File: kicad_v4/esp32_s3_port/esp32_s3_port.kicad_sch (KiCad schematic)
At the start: 50 parts, among them J1 AudioJack4, J2 AudioJack4, SW1 KS33_SW_HS, SW10 KS33_SW_HS, SW11 KS33_SW_HS, SW12 KS33_SW_HS, SW13 KS33_SW_HS, SW14 KS33_SW_HS, SW15 KS33_SW_HS, SW16 KS33_SW_HS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

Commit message: ssd 1306
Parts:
- removed U4: SSD1306-128X64-OLED-0.96, Library:SSD1306, symbol Library:SSD1306-128X64-OLED-0.96
- added Brd1: SSD1306, SSD1306:128x64OLED, symbol ssd1306:SSD1306
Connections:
- net GND: now also Brd1.1 (GND)
- net SCL: now also Brd1.3 (SCL)
- net SDA: now also Brd1.4 (SDA)
- net VCC: now also Brd1.2 (VCC)
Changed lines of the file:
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@@
 	(wire
 		(pts
+			(xy 153.67 121.92) (xy 153.67 127)
+		)
+		(stroke
+			(width 0)
+			(type default)
+		)
+	)
+	(wire
+		(pts
 			(xy 52.07 160.02) (xy 52.07 179.07)
 		)
@@
 	(wire
 		(pts
+			(xy 147.32 127) (xy 151.13 127)
+		)
+		(stroke
+			(width 0)
+			(type default)
+		)
+	)
+	(wire
+		(pts
 			(xy 82.55 172.72) (xy 95.25 172.72)
 		)
@@
 		)
 	)
-	(global_label "SDA"
+	(global_label "RX"
 		(shape input)
-		(at 151.13 140.97 180)
+		(at 156.21 69.85 180)
 		(fields_autoplaced yes)
 		(effects
@@
 		)
 		(property "Intersheetrefs" "${INTERSHEET_REFS}"
-			(at 144.5767 140.97 0)
+			(at 150.7453 69.85 0)
 			(effects
 				(font
@@
 		)
 	)
-	(global_label "RX"
+	(global_label "SCL"
 		(shape input)
-		(at 156.21 69.85 180)
+		(at 156.21 127 90)
 		(fields_autoplaced yes)
 		(effects
@@
 				(size 1.27 1.27)
 			)
-			(justify right)
+			(justify left)
 		)
 		(property "Intersheetrefs" "${INTERSHEET_REFS}"
-			(at 150.7453 69.85 0)
+			(at 156.21 120.5072 90)
 			(effects
 				(font
 					(size 1.27 1.27)
 				)
-				(justify right)
+				(justify left)
 				(hide yes)
 			)
@@
 		)
 	)
-	(global_label "RX"
+	(global_label "SDA"
 		(shape input)
-		(at 106.68 86.36 0)
+		(at 158.75 127 90)
 		(fields_autoplaced yes)
 		(effects
@@
 		)
 		(property "Intersheetrefs" "${INTERSHEET_REFS}"
-			(at 112.1447 86.36 0)
+			(at 158.75 120.4467 90)
 			(effects
 				(font
@@
 		)
 	)
-	(global_label "TX"
+	(global_label "RX"
 		(shape input)
-		(at 106.68 68.58 0)
+		(at 106.68 86.36 0)
 		(fields_autoplaced yes)
 		(effects
@@
 		)
 		(property "Intersheetrefs" "${INTERSHEET_REFS}"
-			(at 111.8423 68.58 0)
+			(at 112.1447 86.36 0)
 			(effects
 				(font
@@
 		)
 	)
-	(global_label "SCL"
+	(global_label "TX"
 		(shape input)
-		(at 151.13 138.43 180)
+		(at 106.68 68.58 0)
 		(fields_autoplaced yes)
 		(effects
@@
 				(size 1.27 1.27)
 			)
-			(justify right)
+			(justify left)
 		)
 		(property "Intersheetrefs" "${INTERSHEET_REFS}"
-			(at 144.6372 138.43 0)
+			(at 111.8423 68.58 0)
 			(effects
 				(font
 					(size 1.27 1.27)
 				)
-				(justify right)
+				(justify left)
 				(hide yes)
 			)
@@
 	)
 	(symbol
-		(lib_id "Library:SSD1306-128X64-OLED-0.96")
-		(at 158.75 140.97 0)
-		(unit 1)
-		(exclude_from_sim no)
-		(in_bom yes)
-		(on_board yes)
-		(dnp no)
-		(fields_autoplaced yes)
-		(property "Reference" "U4"
-			(at 170.18 139.6999 0)
-			(effects
-				(font
-					(size 1.27 1.27)
-				)
-				(justify left)
-			)
-		)
-		(property "Value" "SSD1306-128X64-OLED-0.96"
-			(at 162.052 151.892 0)
-			(effects
-				(font
-					(size 1.27 1.27)
-				)
-				(hide yes)
-			)
-		)
-		(property "Footprint" "Library:SSD1306"
-			(at 160.782 128.778 0)
-			(effects
-				(font
-					(size 1.27 1.27)
-				)
-				(hide yes)
-			)
-		)
-		(property "Datasheet" ""
-			(at 158.75 140.97 0)
-			(effects
-				(font
-					(size 1.27 1.27)
-				)
-				(hide yes)
-			)
-		)
-		(property "Description" ""
-			(at 158.75 140.97 0)
-			(effects
-				(font
-					(size 1.27 1.27)
-				)
-				(hide yes)
-			)
-		)
-		(pin "2"
-		)
-		(pin "1"
-		)
-		(pin "3"
-		)
-		(pin "4"
-		)
-		(instances
-			(project "esp32_s3_port"
-				(path "/b35913c0-3727-49b0-a8b1-477815153830"
-					(reference "U4")
-					(unit 1)
-				)
-			)
-		)
-	)
-	(symbol
 		(lib_id "Device:Battery_Cell")
 		(at 236.22 144.78 0)
@@
 	(symbol
 		(lib_id "power:GND")
-		(at 151.13 146.05 0)
+		(at 147.32 127 0)
 		(unit 1)
 		(exclude_from_sim no)
@@
 		(fields_autoplaced yes)
 		(property "Reference" "#PWR016"
-			(at 151.13 152.4 0)
+			(at 147.32 133.35 0)
 			(effects
 				(font
@@
 		)
 		(property "Value" "GND"
-			(at 151.13 151.13 0)
+			(at 147.32 132.08 0)
 			(effects
 				(font
@@
 		)
 		(property "Footprint" ""
-			(at 151.13 146.05 0)
+			(at 147.32 127 0)
 			(effects
 				(font
@@
 		)
 		(property "Datasheet" ""
-			(at 151.13 146.05 0)
+			(at 147.32 127 0)
 			(effects
 				(font
@@
 		)
 		(property "Description" "Power symbol creates a global label with name \"GND\" , ground"
-			(at 151.13 146.05 0)
+			(at 147.32 127 0)
 			(effects
 				(font
@@
 	(symbol
 		(lib_id "power:VCC")
-		(at 151.13 133.35 0)
+		(at 153.67 121.92 0)
 		(unit 1)
 		(exclude_from_sim no)
@@
 		(fields_autoplaced yes)
 		(property "Reference" "#PWR05"
-			(at 151.13 137.16 0)
+			(at 153.67 125.73 0)
 			(effects
 				(font
@@
 		)
 		(property "Value" "VCC"
-			(at 151.13 128.27 0)
+			(at 153.67 116.84 0)
 			(effects
 				(font
@@
 		)
 		(property "Footprint" ""
-			(at 151.13 133.35 0)
+			(at 153.67 121.92 0)
 			(effects
 				(font
@@
 		)
 		(property "Datasheet" ""
-			(at 151.13 133.35 0)
+			(at 153.67 121.92 0)
 			(effects
 				(font
@@
 		)
 		(property "Description" "Power symbol creates a global label with name \"VCC\""
-			(at 151.13 133.35 0)
+			(at 153.67 121.92 0)
 			(effects
 				(font
@@
 					(unit 1)
 				)
+			)
+		)
+	)
+	(symbol
+		(lib_id "ssd1306:SSD1306")
+		(at 154.94 135.89 0)
+		(unit 1)
+		(exclude_from_sim no)
+		(in_bom yes)
+		(on_board yes)
+		(dnp no)
+		(fields_autoplaced yes)
+		(property "Reference" "Brd1"
+			(at 162.56 134.6199 0)
+			(effects
+				(font
+					(size 1.27 1.27)
+				)
+				(justify left)
+			)
+		)
+		(property "Value" "SSD1306"
+			(at 162.56 137.1599 0)
+			(effects
+				(font
+					(size 1.27 1.27)
+				)
+				(justify left)
+			)
+		)
+		(property "Footprint" "SSD1306:128x64OLED"
+			(at 154.94 129.54 0)
+			(effects
+				(font
+					(size 1.27 1.27)
+				)
+				(hide yes)
+			)
+		)
+		(property "Datasheet" ""
+			(at 154.94 129.54 0)
+			(effects
+				(font
+					(size 1.27 1.27)
+				)
+				(hide yes)
+			)
+		)
+		(property "Description" "SSD1306 OLED"
+			(at 154.94 135.89 0)
+			(effects
+				(font
+					(size 1.27 1.27)
+				)
+				(hide yes)
+			)
+		)
+		(pin "3"
+		)
+		(pin "1"
+		)
+		(pin "2"
+		)
+		(pin "4"
+		)
+		(instances
+			(project ""
+				(path "/b35913c0-3727-49b0-a8b1-477815153830"
+					(reference "Brd1")
+					(unit 1)
+				)

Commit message: battery switch
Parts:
- added SW22: Slide_Switch_SPDT_P3mm_10x5x10mm, PCM_SL_Devices:Slide_Switch_SPDT_P3mm_10x5x10mm, symbol PCM_SL_Devices:Slide_Switch_SPDT_P3mm_10x5x10mm
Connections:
- net at BT1.1 (+), JP1.1: now also SW22.2; no longer U1.3 (BAT)
- new net: SW22.1, U1.3 (BAT)
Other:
- moved on the sheet: BT1, JP1
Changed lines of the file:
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@@
 	)
 	(junction
-		(at 231.14 139.7)
-		(diameter 0)
-		(color 0 0 0 0)
-	)
-	(junction
 		(at 44.45 172.72)
 		(diameter 0)
@@
 	)
 	(junction
+		(at 243.84 138.43)
+		(diameter 0)
+		(color 0 0 0 0)
+	)
+	(junction
 		(at 69.85 137.16)
 		(diameter 0)
@@
 	)
 	(junction
-		(at 236.22 147.32)
+		(at 246.38 146.05)
 		(diameter 0)
 		(color 0 0 0 0)
@@
 	(wire
 		(pts
+			(xy 243.84 137.16) (xy 243.84 138.43)
+		)
+		(stroke
+			(width 0)
+			(type default)
+		)
+	)
+	(wire
+		(pts
 			(xy 26.67 140.97) (xy 26.67 160.02)
 		)
@@
 	(wire
 		(pts
+			(xy 243.84 138.43) (xy 246.38 138.43)
+		)
+		(stroke
+			(width 0)
+			(type default)
+		)
+	)
+	(wire
+		(pts
 			(xy 156.21 72.39) (xy 161.29 72.39)
 		)
@@
 	(wire
 		(pts
-			(xy 231.14 139.7) (xy 236.22 139.7)
+			(xy 241.3 138.43) (xy 243.84 138.43)
 		)
 		(stroke
@@
 	(wire
 		(pts
-			(xy 220.98 139.7) (xy 231.14 139.7)
+			(xy 69.85 153.67) (xy 82.55 153.67)
 		)
 		(stroke
@@
 	(wire
 		(pts
-			(xy 69.85 153.67) (xy 82.55 153.67)
+			(xy 31.75 172.72) (xy 44.45 172.72)
 		)
 		(stroke
@@
 	(wire
 		(pts
-			(xy 31.75 172.72) (xy 44.45 172.72)
+			(xy 52.07 115.57) (xy 52.07 124.46)
 		)
 		(stroke
@@
 	(wire
 		(pts
-			(xy 52.07 115.57) (xy 52.07 124.46)
+			(xy 39.37 114.3) (xy 39.37 124.46)
 		)
 		(stroke
@@
 	(wire
 		(pts
-			(xy 39.37 114.3) (xy 39.37 124.46)
+			(xy 69.85 137.16) (xy 82.55 137.16)
 		)
 		(stroke
@@
 	(wire
 		(pts
-			(xy 69.85 137.16) (xy 82.55 137.16)
+			(xy 64.77 124.46) (xy 64.77 140.97)
 		)
 		(stroke
@@
 	(wire
 		(pts
-			(xy 64.77 124.46) (xy 64.77 140.97)
+			(xy 232.41 137.16) (xy 243.84 137.16)
 		)
 		(stroke
@@
 	(wire
 		(pts
-			(xy 231.14 147.32) (xy 231.14 146.05)
+			(xy 241.3 146.05) (xy 241.3 144.78)
 		)
 		(stroke
@@
 	(wire
 		(pts
-			(xy 231.14 139.7) (xy 231.14 140.97)
+			(xy 241.3 138.43) (xy 241.3 139.7)
 		)
 		(stroke
@@
 	(wire
 		(pts
-			(xy 236.22 149.86) (xy 236.22 147.32)
+			(xy 246.38 148.59) (xy 246.38 146.05)
 		)
 		(stroke
@@
 	(wire
 		(pts
-			(xy 231.14 147.32) (xy 236.22 147.32)
+			(xy 241.3 146.05) (xy 246.38 146.05)
 		)
 		(stroke
@@
 	(symbol
 		(lib_id "power:GND")
-		(at 236.22 149.86 0)
+		(at 246.38 148.59 0)
 		(unit 1)
 		(exclude_from_sim no)
@@
 		(fields_autoplaced yes)
 		(property "Reference" "#PWR02"
-			(at 236.22 156.21 0)
+			(at 246.38 154.94 0)
 			(effects
 				(font
@@
 		)
 		(property "Value" "GND"
-			(at 236.22 154.94 0)
+			(at 246.38 153.67 0)
 			(effects
 				(font
@@
 		)
 		(property "Footprint" ""
-			(at 236.22 149.86 0)
+			(at 246.38 148.59 0)
 			(effects
 				(font
@@
 		)
 		(property "Datasheet" ""
-			(at 236.22 149.86 0)
+			(at 246.38 148.59 0)
 			(effects
 				(font
@@
 		)
 		(property "Description" "Power symbol creates a global label with name \"GND\" , ground"
-			(at 236.22 149.86 0)
+			(at 246.38 148.59 0)
 			(effects
 				(font
@@
 	(symbol
 		(lib_id "Device:Battery_Cell")
-		(at 236.22 144.78 0)
+		(at 246.38 143.51 0)
 		(unit 1)
 		(exclude_from_sim no)
@@
 		(fields_autoplaced yes)
 		(property "Reference" "BT1"
-			(at 240.03 141.6684 0)
+			(at 250.19 140.3984 0)
 			(effects
 				(font
@@
 		)
 		(property "Value" "Battery_Cell"
-			(at 240.03 144.2084 0)
+			(at 250.19 142.9384 0)
 			(effects
 				(font
@@
 		)
 		(property "Footprint" ""
-			(at 236.22 143.256 90)
+			(at 246.38 141.986 90)
 			(effects
 				(font
@@
 		)
 		(property "Datasheet" "~"
-			(at 236.22 143.256 90)
+			(at 246.38 141.986 90)
 			(effects
 				(font
@@
 		)
 		(property "Description" "Single-cell battery"
-			(at 236.22 144.78 0)
+			(at 246.38 143.51 0)
 			(effects
 				(font
@@
 		(on_board yes)
 		(dnp no)
-		(fields_autoplaced yes)
 		(property "Reference" "R2"
 			(at 226.06 147.3199 90)
@@
 		)
 		(property "Value" "2.2k"
-			(at 226.06 149.8599 90)
+			(at 236.22 148.5899 90)
 			(effects
 				(font
@@
 	(symbol
 		(lib_id "PCM_SL_Jumpers_THT:JUP_P5.08mm")
-		(at 231.14 143.51 270)
+		(at 241.3 142.24 270)
 		(unit 1)
 		(exclude_from_sim no)
@@
 		(fields_autoplaced yes)
 		(property "Reference" "JP1"
-			(at 232.41 142.24 90)
+			(at 242.57 140.97 90)
 			(effects
 				(font
@@
 		)
 		(property "Value" "JUP_P5.08mm"
-			(at 232.41 144.78 90)
+			(at 242.57 143.51 90)
 			(effects
 				(font
@@
 		)
 		(property "Footprint" "PCM_SL_Jumpers:JUP_P5.08mm"
-			(at 231.14 143.51 0)
+			(at 241.3 142.24 0)
 			(effects
 				(font
@@
 		)
 		(property "Datasheet" ""
-			(at 231.14 143.51 0)
+			(at 241.3 142.24 0)
 			(effects
 				(font
@@
 		)
 		(property "Description" "Through-Hole Jumpers or wire links with a pin space of 5.08mm"
-			(at 231.14 143.51 0)
+			(at 241.3 142.24 0)
 			(effects
 				(font
@@
 					(unit 1)
 				)
+			)
+		)
+	)
+	(symbol
+		(lib_id "PCM_SL_Devices:Slide_Switch_SPDT_P3mm_10x5x10mm")
+		(at 227.33 139.7 0)
+		(unit 1)
+		(exclude_from_sim no)
+		(in_bom yes)
+		(on_board yes)
+		(dnp no)
+		(fields_autoplaced yes)
+		(property "Reference" "SW22"
+			(at 226.695 132.08 0)
+			(effects
+				(font
+					(size 1.27 1.27)
+				)
+			)
+		)
+		(property "Value" "Slide_Switch_SPDT_P3mm_10x5x10mm"
+			(at 226.695 134.62 0)
+			(effects
+				(font
+					(size 1.27 1.27)
+				)
+			)
+		)
+		(property "Footprint" "PCM_SL_Devices:Slide_Switch_SPDT_P3mm_10x5x10mm"
+			(at 228.6 147.32 0)
+			(effects
+				(font
+					(size 1.27 1.27)
+				)
+				(hide yes)
+			)
+		)
+		(property "Datasheet" ""
+			(at 226.06 133.35 0)
+			(effects
+				(font
+					(size 1.27 1.27)
+				)
+				(hide yes)
+			)
+		)
+		(property "Description" "SPDT Slide Switch with 10mm length, 5mm width and 10mm hight."
+			(at 227.33 139.7 0)
+			(effects
+				(font
+					(size 1.27 1.27)
+				)
+				(hide yes)
+			)
+		)
+		(pin "1"
+		)
+		(pin "2"
+		)
+		(pin "3"
+		)
+		(instances
+			(project ""
+				(path "/b35913c0-3727-49b0-a8b1-477815153830"
+					(reference "SW22")
+					(unit 1)
+				)

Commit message: updates
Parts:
- removed BT1: Battery_Cell, symbol Device:Battery_Cell
- removed J1, J2: AudioJack4, PJ-320A_Library:PJ-320A, symbol TRRS:AudioJack4
- removed JP1: JUP_P5.08mm, PCM_SL_Jumpers:JUP_P5.08mm, symbol PCM_SL_Jumpers_THT:JUP_P5.08mm
- added J1: Battery, Connector_PinHeader_2.54mm:PinHeader_1x02_P2.54mm_Vertical, symbol PCM_SL_Pin_Headers:PINHD_1x2_Male
- added J3: misc Pogo pin connector, Connector_PinHeader_2.54mm:PinHeader_1x04_P2.54mm_Vertical, symbol PCM_SL_Pin_Headers:PINHD_1x4_Male
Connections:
- net GND: now also J1.2, J3.4
- net SCL: now also J3.2
- net SDA: now also J3.3
- net VCC: now also J3.1
- net at SW22.2: now also J1.1
- net RX: no longer names the net of A1.2 (D0/RX)
- net TX: no longer names the net of A1.1 (D1/TX)
- net VBUS: no longer names the net of A1.27 (VUSB/5V)
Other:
- moved on the sheet: A1, Brd1, D1, D10, D11, D12, D13, D14, D15, D16, D17, D18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

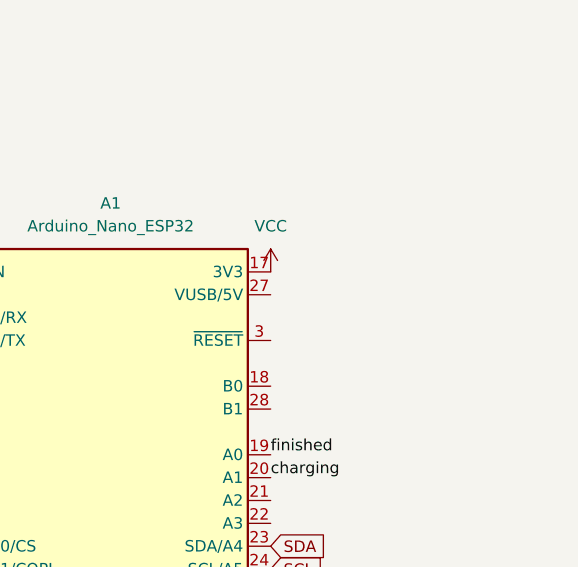
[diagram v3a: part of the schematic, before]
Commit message: hardware update
lots of items were switced with the equivalent headers
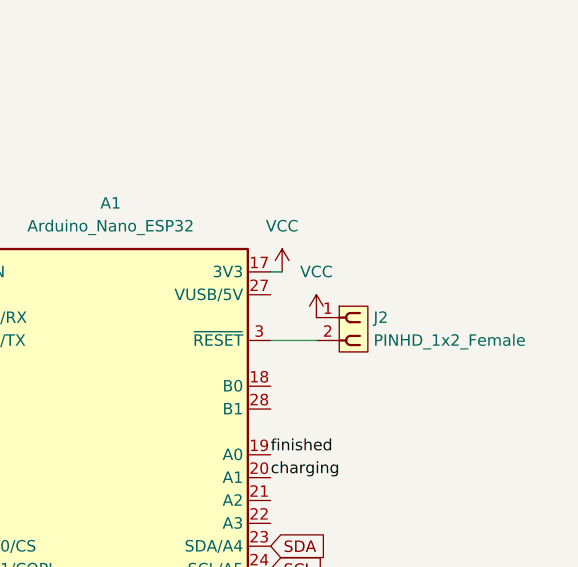
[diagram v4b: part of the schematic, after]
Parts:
- added J2: PINHD_1x2_Female, Connector_PinSocket_2.54mm:PinSocket_1x02_P2.54mm_Vertical, symbol PCM_SL_Pin_Headers:PINHD_1x2_Female
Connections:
- net VCC: now also J2.1
- net at A1.3 (~{RESET}): now also J2.2
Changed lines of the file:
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@@
 	(wire
 		(pts
+			(xy 237.49 82.55) (xy 242.57 82.55)
+		)
+		(stroke
+			(width 0)
+			(type default)
+		)
+	)
+	(wire
+		(pts
 			(xy 139.7 22.86) (xy 139.7 25.4)
 		)
@@
 	(wire
 		(pts
+			(xy 238.76 74.93) (xy 237.49 74.93)
+		)
+		(stroke
+			(width 0)
+			(type default)
+		)
+	)
+	(wire
+		(pts
 			(xy 69.85 77.47) (xy 82.55 77.47)
 		)
@@
 	)
 	(symbol
+		(lib_id "power:VCC")
+		(at 242.57 80.01 0)
+		(unit 1)
+		(exclude_from_sim no)
+		(in_bom yes)
+		(on_board yes)
+		(dnp no)
+		(fields_autoplaced yes)
+		(property "Reference" "#PWR08"
+			(at 242.57 83.82 0)
+			(effects
+				(font
+					(size 1.27 1.27)
+				)
+				(hide yes)
+			)
+		)
+		(property "Value" "VCC"
+			(at 242.57 74.93 0)
+			(effects
+				(font
+					(size 1.27 1.27)
+				)
+			)
+		)
+		(property "Footprint" ""
+			(at 242.57 80.01 0)
+			(effects
+				(font
+					(size 1.27 1.27)
+				)
+				(hide yes)
+			)
+		)
+		(property "Datasheet" ""
+			(at 242.57 80.01 0)
+			(effects
+				(font
+					(size 1.27 1.27)
+				)
+				(hide yes)
+			)
+		)
+		(property "Description" "Power symbol creates a global label with name \"VCC\""
+			(at 242.57 80.01 0)
+			(effects
+				(font
+					(size 1.27 1.27)
+				)
+				(hide yes)
+			)
+		)
+		(pin "1"
+		)
+		(instances
+			(project "esp32_s3_port"
+				(path "/b35913c0-3727-49b0-a8b1-477815153830"
+					(reference "#PWR08")
+					(unit 1)
+				)
+			)
+		)
+	)
+	(symbol
 		(lib_id "PCM_marbastlib-gateron_lp:KS33_SW_HS_KS-2P02B01-02")
 		(at 80.01 31.75 0)
@@
 	(symbol
 		(lib_id "power:VCC")
-		(at 237.49 74.93 0)
+		(at 238.76 74.93 0)
 		(unit 1)
 		(exclude_from_sim no)
@@
 		(fields_autoplaced yes)
 		(property "Reference" "#PWR04"
-			(at 237.49 78.74 0)
+			(at 238.76 78.74 0)
 			(effects
 				(font
@@
 		)
 		(property "Value" "VCC"
-			(at 237.49 69.85 0)
+			(at 238.76 69.85 0)
 			(effects
 				(font
@@
 		)
 		(property "Footprint" ""
-			(at 237.49 74.93 0)
+			(at 238.76 74.93 0)
 			(effects
 				(font
@@
 		)
 		(property "Datasheet" ""
-			(at 237.49 74.93 0)
+			(at 238.76 74.93 0)
 			(effects
 				(font
@@
 		)
 		(property "Description" "Power symbol creates a global label with name \"VCC\""
-			(at 237.49 74.93 0)
+			(at 238.76 74.93 0)
 			(effects
 				(font
@@
 					(unit 1)
 				)
+			)
+		)
+	)
+	(symbol
+		(lib_id "PCM_SL_Pin_Headers:PINHD_1x2_Female")
+		(at 246.38 81.28 0)
+		(unit 1)
+		(exclude_from_sim no)
+		(in_bom yes)
+		(on_board yes)
+		(dnp no)
+		(fields_autoplaced yes)
+		(property "Reference" "J2"
+			(at 248.92 80.0099 0)
+			(effects
+				(font
+					(size 1.27 1.27)
+				)
+				(justify left)
+			)
+		)
+		(property "Value" "PINHD_1x2_Female"
+			(at 248.92 82.5499 0)
+			(effects
+				(font
+					(size 1.27 1.27)
+				)
+				(justify left)
+			)
+		)
+		(property "Footprint" "Connector_PinSocket_2.54mm:PinSocket_1x02_P2.54mm_Vertical"
+			(at 248.92 71.12 0)
+			(effects
+				(font
+					(size 1.27 1.27)
+				)
+				(hide yes)
+			)
+		)
+		(property "Datasheet" ""
+			(at 246.38 73.66 0)
+			(effects
+				(font
+					(size 1.27 1.27)
+				)
+				(hide yes)
+			)
+		)
+		(property "Description" "Pin Header female with pin space 2.54mm. Pin Count -2"
+			(at 246.38 81.28 0)
+			(effects
+				(font
+					(size 1.27 1.27)
+				)
+				(hide yes)
+			)
+		)
+		(pin "1"
+		)
+		(pin "2"
+		)
+		(instances
+			(project ""
+				(path "/b35913c0-3727-49b0-a8b1-477815153830"
+					(reference "J2")
+					(unit 1)
+				)
